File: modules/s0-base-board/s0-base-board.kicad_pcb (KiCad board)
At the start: 2 copper layers, 54.6 x 86.4 mm, 64 parts, among them J1 USB_C_Receptacle_USB2.0_14P, J2 Screw_Terminal_01x02, J3 BAT_JST_01x02, J4 RJ45_Bel_SI-60062-F JLC(C3467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, J5 Conn_02x23_Odd_Even, J6 Conn_02x23_Odd_Even, Q1 PMOS, U1 MCP73831-2-OT, U2 XL1509-5.0, U3 LM2575-3.3BU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

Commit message: Production build
Signed-off-by: Rodney Osodo <socials@rodneyosodo.com>
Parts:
- removed J1: USB_C_Receptacle_USB2.0_14P, Connector_USB:USB_C_Receptacle_G-Switch_GT-USB-7010ASV
- removed R2, R3: 5K1, Resistor_SMD:R_0603_1608Metric
- C10, C13, C14, C9: footprint Capacitor_SMD:C_0603_1608Metric -> Capacitor_SMD:C_0402_1005Metric
- C12: footprint Capacitor_SMD:C_0603_1608Metric -> Capacitor_SMD:C_0805_2012Metric
- C16: value 4.7uF -> 0.1uF; footprint Capacitor_SMD:C_0603_1608Metric -> Capacitor_SMD:C_0402_1005Metric
- C17: value 10nF -> 4.7uF
- C21: value 0.1uF -> 10uF; footprint Capacitor_SMD:C_0603_1608Metric -> Capacitor_SMD:C_0805_2012Metric
- C22: value 10uF -> 10nF
- C4, C5: value 680uF -> 10uF; footprint Capacitor_SMD:C_0603_1608Metric -> Capacitor_SMD:C_0805_2012Metric
- C6, C7: footprint Capacitor_SMD:C_0603_1608Metric -> Capacitor_SMD:C_1206_3216Metric
- D1: footprint LED_SMD:LED_1206_3216Metric -> LED_SMD:LED_0603_1608Metric
- D2, D3, D4: value D -> 40V 3A 550mV@3A Schottky; footprint Diode_SMD:D_0603_1608Metric -> Diode_SMD:D_SMA-SMB_Universal_Handsoldering
- J2: footprint TerminalBlock:TerminalBlock_Xinya_XY308-2.54-2P_1x02_P2.54mm_Horizontal -> TerminalBlock:TerminalBlock_MaiXu_MX126-5.0-02P_1x02_P5.00mm
- J4: value RJ45_Bel_SI-60062-F JLC(C34677) -> RJ45_Bel_SI-60062-F JLC
- J5, J6: footprint Connector_PinHeader_2.54mm:PinHeader_2x23_P2.54mm_Vertical -> Connector_PinSocket_2.54mm:PinSocket_2x23_P2.54mm_Vertical
- L1: value 68uH/2A -> 47uH/2A; footprint Inductor_SMD:L_0201_0603Metric -> Inductor_SMD:L_Chilisin_BMRB00060624
- L2: value 33uH -> 47uH/2A; footprint Inductor_SMD:L_0201_0603Metric -> Inductor_SMD:L_Chilisin_BMRB00060624
- L3: footprint Inductor_SMD:L_0201_0603Metric -> Inductor_SMD:L_0603_1608Metric
- R1, R19: footprint Resistor_SMD:R_0603_1608Metric -> Resistor_SMD:R_0402_1005Metric
- R4: value 2k -> 100; footprint Resistor_SMD:R_0603_1608Metric -> Resistor_SMD:R_0402_1005Metric
- R9: value 12.4K 1% -> 12K 1%
- U3: value LM2575-3.3BU -> LM2575S-3.3(UMW)
- Y1: footprint Crystal:Crystal_SMD_2520-4Pin_2.5x2.0mm -> Crystal:Crystal_SMD_3225-4Pin_3.2x2.5mm
- moved U5 103.0 mm to (202.6, 73.3)
- moved L2 97.7 mm to (197.9, 110.2), turned to 0 degrees
- moved C16 88.7 mm to (191.9, 88.5), turned to 90 degrees
- moved D1 79.1 mm to (206.3, 53.5)
- moved C1 77.7 mm to (203.6, 59.9)
- moved R4 77.7 mm to (203.1, 53.4)
- moved U1 77.7 mm to (203.1, 57.0)
- moved R1 77.7 mm to (206.6, 57.1)
- moved U3 77.6 mm to (192.8, 121.3)
- moved J5 77.4 mm to (210.8, 62.6)
- moved C7 77.3 mm to (179.2, 123.0), turned to 180 degrees
- moved C20 76.8 mm to (195.3, 73.6)
- moved C3 76.8 mm to (197.8, 69.5)
- moved R10 76.8 mm to (187.4, 74.2)
- moved R11 76.8 mm to (187.3, 68.7)
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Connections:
- C16 pad 1: Net-(U4-TOCAP) -> VCCA
- C17 pad 1: GND -> Net-(U4-TOCAP)
- C17 pad 2: Net-(J4-RCT) -> GND
- C22 pad 1: VCCA -> Net-(J4-RCT)
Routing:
- net +5V: track 154.6 -> 113.9 mm, vias 4 -> 1
- net Net-(D3-K): track 21.8 -> 53.5 mm
- net VIN: track 63.9 -> 32.4 mm
- net Net-(D4-K): track 6.96 -> 37.3 mm, vias 0 -> 2
- net Net-(J4-TD+): track 51.3 -> 25.4 mm, vias 1 -> 0
- net VBAT: track 87.9 -> 73.4 mm
- net +3V3: track 105.9 -> 120.1 mm, vias 4 -> 3
- net TXN: track 27.9 -> 15.2 mm
- net Net-(J4-TD-): track 44.0 -> 33.0 mm, vias 1 -> 0
- net MOSI: track 28.8 -> 20.4 mm
- net Net-(D2-K): track 5.85 -> 13.7 mm
- net VCCA: track 44.5 -> 38.8 mm
- net Net-(J1-CC1): track 4.64 -> 0.00 mm
- net Net-(J1-CC2): track 4.52 -> 0.00 mm
- net CS: track 26.5 -> 22.2 mm
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- added copper zone on B.Cu, net GND
- added copper zone on F.Cu, net GND
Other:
- outline, holes or cut-outs redrawn

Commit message: Documentation added onto Schematic
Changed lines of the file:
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@@
 		(tags "Diode Universal SMA (DO-214AC) SMB (DO-214AA) Handsoldering ")
 		(property "Reference" "D4"
-			(at 0 -3 0)
+			(at 0.55 2.95 0)
 			(layer "F.SilkS")
 			(effects

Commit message: feat(base): add schematic notes and PCB notes
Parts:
- added kibuzzard-67D30BA5: G***, kibuzzard-67D30BA5, F.Cu at (161.2, 49.6)
- added kibuzzard-67D30BB5: G***, kibuzzard-67D30BB5, F.Cu at (175.4, 49.9)
- added kibuzzard-67D30C33: G***, kibuzzard-67D30C33, F.Cu at (207.6, 49.7)
- added kibuzzard-67D30C9E: G***, kibuzzard-67D30C9E, F.Cu at (203.1, 49.7)
- added kibuzzard-67D30CE3: G***, kibuzzard-67D30CE3, F.Cu at (204.7, 92.7)
- added kibuzzard-67D30CF0: G***, kibuzzard-67D30CF0, F.Cu at (204.7, 95.2)
- added kibuzzard-67D30CFC: G***, kibuzzard-67D30CFC, F.Cu at (204.8, 97.9)
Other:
- board text added: "JLCJLCJLCJLC"

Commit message: chore: Updated BOM and PCB
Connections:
- J5 pad 29: MISO -> (no net)
- J5 pad 30: MOSI -> (no net)
- J5 pad 31: SCLK -> (no net)
- J5 pad 32: CS -> (no net)
- J5 pad 33: INT -> (no net)
- J5 pad 34: RST -> (no net)
- J6 pad 29: unconnected-(J6-Pin_29-Pad29) -> MISO
- J6 pad 30: unconnected-(J6-Pin_30-Pad30) -> MOSI
- J6 pad 31: unconnected-(J6-Pin_31-Pad31) -> SCLK
- J6 pad 32: unconnected-(J6-Pin_32-Pad32) -> CS
- J6 pad 33: unconnected-(J6-Pin_33-Pad33) -> INT
- J6 pad 34: unconnected-(J6-Pin_34-Pad34) -> RST
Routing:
- net RST: track 22.3 -> 37.9 mm
- net MOSI: track 20.4 -> 33.4 mm
- net CS: track 22.2 -> 35.0 mm
- net MISO: track 25.3 -> 30.6 mm
- net SCLK: track 24.7 -> 28.4 mm
- net INT: track 26.7 -> 30.3 mm

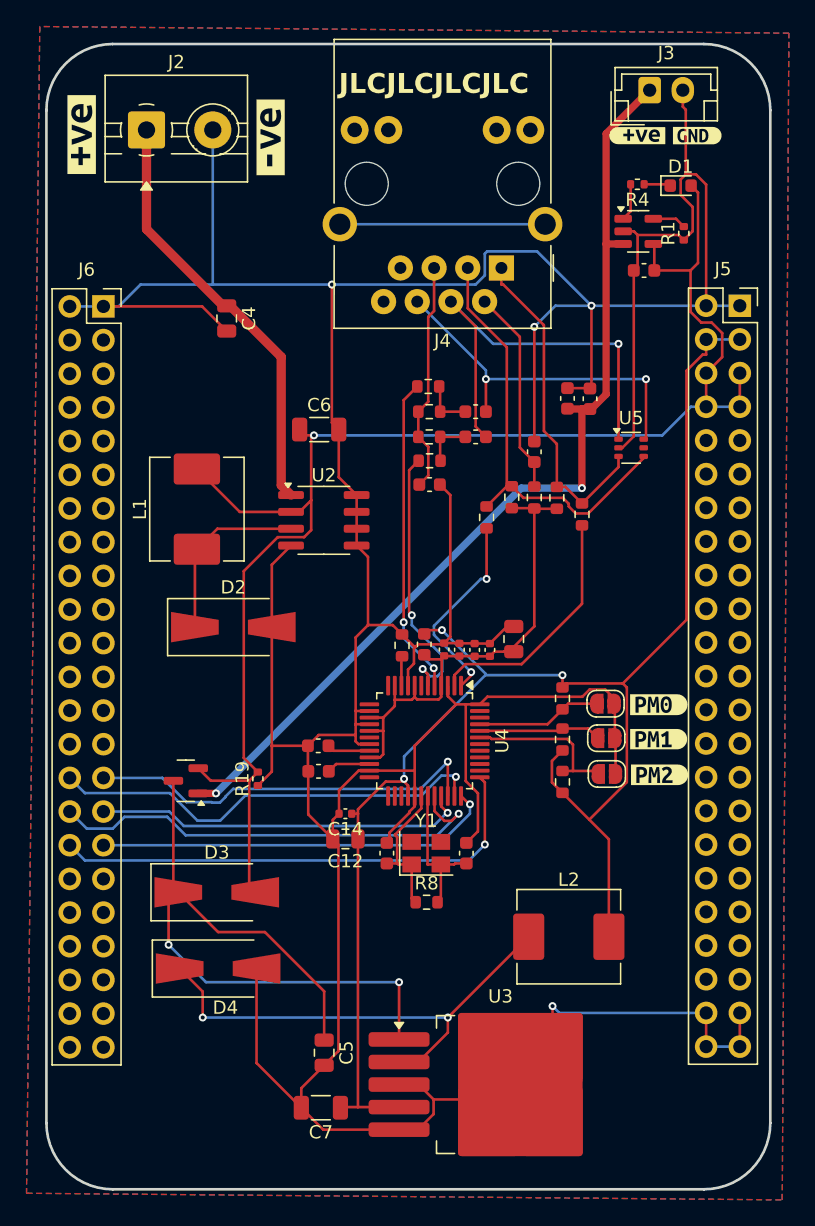
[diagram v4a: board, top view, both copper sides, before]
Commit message: JLCPCB Modified parts
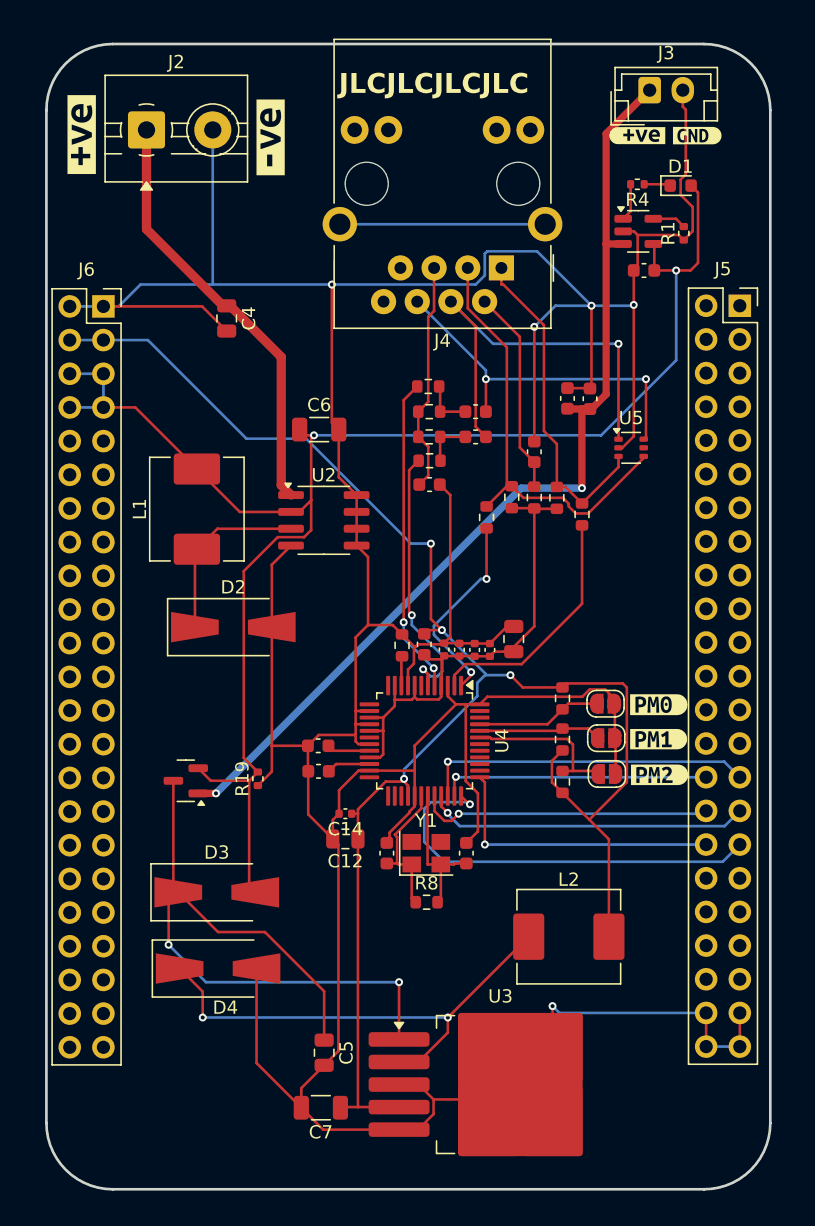
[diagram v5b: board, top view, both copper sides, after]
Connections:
- J5 pad 1: GND -> (no net)
- J5 pad 2: GND -> (no net)
- J5 pad 29: (no net) -> MISO
- J5 pad 3: +3V3 -> (no net)
- J5 pad 30: (no net) -> MOSI
- J5 pad 31: (no net) -> SCLK
- J5 pad 32: (no net) -> CS
- J5 pad 33: (no net) -> INT
- J5 pad 34: (no net) -> RST
- J5 pad 4: +3V3 -> (no net)
- J5 pad 5: +5V -> (no net)
- J5 pad 6: +5V -> (no net)
- J5 pad 7: +5V -> (no net)
- J5 pad 8: +5V -> (no net)
- J6 pad 29: MISO -> (no net)
- J6 pad 3: unconnected-(J6-Pin_3-Pad3) -> +3V3
- J6 pad 30: MOSI -> (no net)
- J6 pad 31: SCLK -> (no net)
- J6 pad 32: CS -> (no net)
- J6 pad 33: INT -> (no net)
- J6 pad 34: RST -> (no net)
- J6 pad 4: unconnected-(J6-Pin_4-Pad4) -> +3V3
- J6 pad 5: unconnected-(J6-Pin_5-Pad5) -> +5V
- J6 pad 6: unconnected-(J6-Pin_6-Pad6) -> +5V
- J6 pad 7: unconnected-(J6-Pin_7-Pad7) -> +5V
- J6 pad 8: unconnected-(J6-Pin_8-Pad8) -> +5V
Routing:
- net GND: track 391.3 -> 372.4 mm, vias 4 -> 5
- net RST: track 37.9 -> 22.3 mm
- net MOSI: track 33.4 -> 20.5 mm
- net CS: track 35.0 -> 22.2 mm
- net +3V3: track 120.1 -> 128.8 mm, vias 3 -> 4
- net MISO: track 30.6 -> 25.1 mm
- net +5V: track 113.9 -> 119.1 mm, vias 1 -> 2
- net SCLK: track 28.4 -> 24.6 mm
- net INT: track 30.3 -> 32.1 mm
- removed copper zone on B.Cu, net GND
- removed copper zone on F.Cu, net GND

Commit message: BaseBoard Modification
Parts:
- added D5: 40V 3A 550mV@3A Schottky, Diode_SMD:D_SMA-SMB_Universal_Handsoldering, F.Cu at (165.6, 55.5)
- added D6: BZV55C27, Diode_SMD:D_MiniMELF, F.Cu at (170.5, 64.0)
- added G***: LOGO, Absmach:absmach1, F.Cu at (206.0, 124.0)
- added L4: L_Ferrite, Inductor_SMD:L_0603_1608Metric, F.Cu at (179.0, 93.5)
- added Q2: DMP3013SFV, Package_SON:Diodes_PowerDI3333-8, F.Cu at (175.0, 61.5)
- added Q3: DMP3013SFV, Package_SON:Diodes_PowerDI3333-8, F.Cu at (173.5, 56.0)
- added R2: 1.2k, Resistor_SMD:R_0402_1005Metric, F.Cu at (167.5, 59.0)
- added R20: 330, Resistor_SMD:R_0402_1005Metric, F.Cu at (177.0, 55.0)
- added R21: 330, Resistor_SMD:R_0402_1005Metric, F.Cu at (199.0, 46.0)
- added R22: 10k, Resistor_SMD:R_0402_1005Metric, F.Cu at (180.5, 99.5)
- added R23: 10k, Resistor_SMD:R_0402_1005Metric, F.Cu at (193.0, 103.0)
- added R24: 10k, Resistor_SMD:R_0402_1005Metric, F.Cu at (194.5, 103.0)
- added R25: 10k, Resistor_SMD:R_0402_1005Metric, F.Cu at (196.5, 103.0)
- added R26: 10k, Resistor_SMD:R_0402_1005Metric, F.Cu at (197.5, 103.0)
- added R27: 10k, Resistor_SMD:R_0402_1005Metric, F.Cu at (198.5, 103.0)
- added R3: 1.2k, Resistor_SMD:R_0402_1005Metric, F.Cu at (177.5, 64.5)
- C6: value 220uF -> 330uF
- R19: value 100k -> 10k
- R4: value 100 -> 220
- moved C4 7.12 mm to (178.0, 67.5), turned to 0 degrees
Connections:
- J2 pad 1: VIN -> Net-(D5-A)
- J4 pad L1: unconnected-(J4-PadL1) -> Net-(J4-PadL1)
- J4 pad L2: unconnected-(J4-PadL2) -> GND
- J4 pad L3: unconnected-(J4-PadL3) -> Net-(J4-PadL3)
- J4 pad L4: unconnected-(J4-PadL4) -> GND
- J4 pad SH: unconnected-(J4-PadSH) -> GND
- J5 pad 1: (no net) -> GND
- J5 pad 2: (no net) -> GND
- J6 pad 29: (no net) -> unconnected-(J6-Pin_29-Pad29)
- J6 pad 30: (no net) -> unconnected-(J6-Pin_30-Pad30)
- J6 pad 31: (no net) -> unconnected-(J6-Pin_31-Pad31)
- J6 pad 32: (no net) -> unconnected-(J6-Pin_32-Pad32)
- J6 pad 33: (no net) -> unconnected-(J6-Pin_33-Pad33)
- J6 pad 34: (no net) -> unconnected-(J6-Pin_34-Pad34)
- U4 pad 23: GND -> Net-(R22-Pad2)
- U4 pad 38: unconnected-(U4-RSVD-Pad38) -> Net-(R23-Pad2)
- U4 pad 39: unconnected-(U4-RSVD-Pad39) -> Net-(R24-Pad2)
- U4 pad 40: unconnected-(U4-RSVD-Pad40) -> Net-(R25-Pad2)
- U4 pad 41: unconnected-(U4-RSVD-Pad41) -> Net-(R26-Pad2)
- U4 pad 42: unconnected-(U4-RSVD-Pad42) -> Net-(R27-Pad2)
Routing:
- net ACTLED: track 0.00 -> 68.7 mm, vias 0 -> 4
- net LINKLED: track 0.00 -> 64.4 mm, vias 0 -> 4
- net GND: track 372.4 -> 420.1 mm
- net Net-(D6-K): track 0.00 -> 32.9 mm, vias 0 -> 2
- net VIN: track 32.4 -> 16.5 mm
- net unconnected-(J4-PadSH): track 15.5 -> 0.00 mm
- net Net-(D5-K): track 0.00 -> 14.7 mm
- net +3V3: track 128.8 -> 141.5 mm, vias 4 -> 5
- net Net-(J4-PadL3): track 0.00 -> 11.9 mm
- net Net-(Q2-G): track 0.00 -> 11.9 mm
- net Net-(R27-Pad2): track 0.00 -> 11.3 mm
- net Net-(R26-Pad2): track 0.00 -> 10.1 mm
- net Net-(R25-Pad2): track 0.00 -> 9.12 mm
- net Net-(D5-A): track 0.00 -> 7.59 mm
- net Net-(R24-Pad2): track 0.00 -> 7.58 mm
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
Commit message: Logo update
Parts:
- removed the G*** at (206.0, 124.0)
- added G***: LOGO, LOGO, B.Cu at (187.5, 85.0)

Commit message: Updated Logo
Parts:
- removed Q2, Q3: DMP3013SFV, Package_SON:Diodes_PowerDI3333-8
- removed R2, R3: 1.2k, Resistor_SMD:R_0402_1005Metric
- moved G*** 3.20 mm to (185.5, 82.5)
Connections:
- D5 pad 1: Net-(D5-K) -> VIN
- D6 pad 1: Net-(D6-K) -> VIN
- J5 pad 3: (no net) -> +3V3
- J5 pad 4: (no net) -> +3V3
- J5 pad 5: (no net) -> +5V
- J5 pad 6: (no net) -> +5V
- J5 pad 7: (no net) -> +5V
- J5 pad 8: (no net) -> +5V
- J6 pad 3: +3V3 -> unconnected-(J6-Pin_3-Pad3)
- J6 pad 4: +3V3 -> unconnected-(J6-Pin_4-Pad4)
- J6 pad 5: +5V -> unconnected-(J6-Pin_5-Pad5)
- J6 pad 6: +5V -> unconnected-(J6-Pin_6-Pad6)
- J6 pad 7: +5V -> unconnected-(J6-Pin_7-Pad7)
- J6 pad 8: +5V -> unconnected-(J6-Pin_8-Pad8)
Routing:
- net Net-(D6-K): track 32.9 -> 0.00 mm, vias 2 -> 0
- net Net-(D5-K): track 14.7 -> 0.00 mm
- net Net-(Q2-G): track 11.9 -> 0.00 mm
- net VIN: track 16.5 -> 27.8 mm
- net GND: track 420.1 -> 417.7 mm
- added copper zone on B.Cu, net GND
- added copper zone on F.Cu, net GND
